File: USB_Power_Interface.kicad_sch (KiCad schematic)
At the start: 33 parts, among them CN501 GT-USB-7014D, U501 TPS2121, U502 TPSM82903

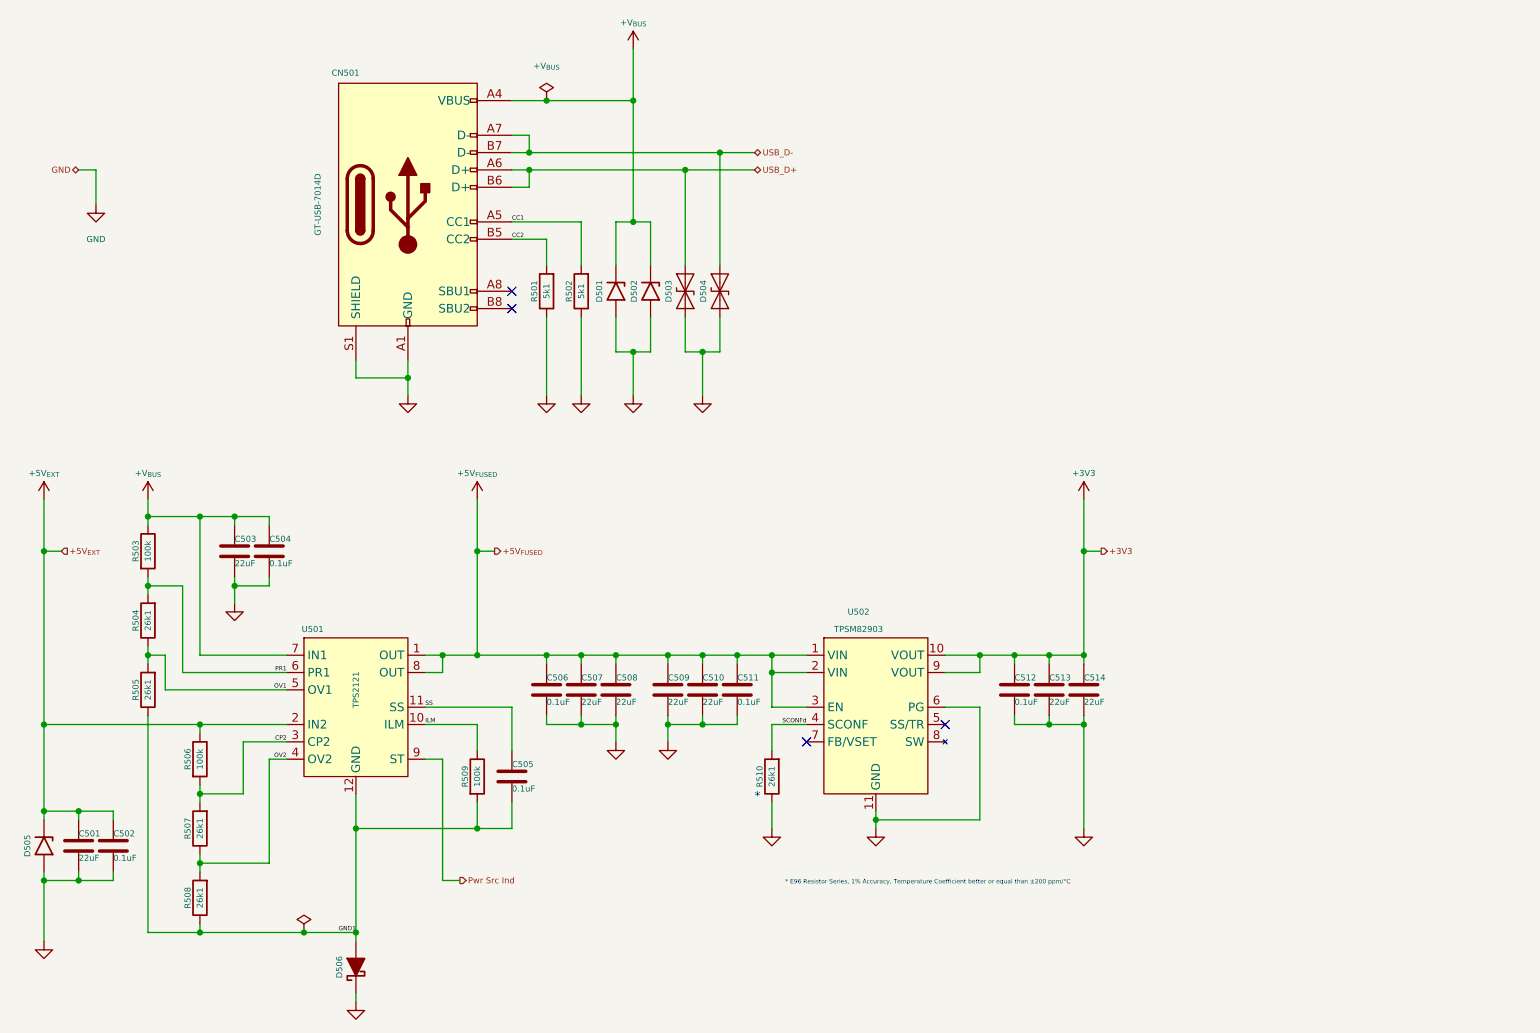
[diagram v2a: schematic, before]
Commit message: fixed hierarchical sheets; replaced pin headers with ESP32-S3_D1_Pico symbol
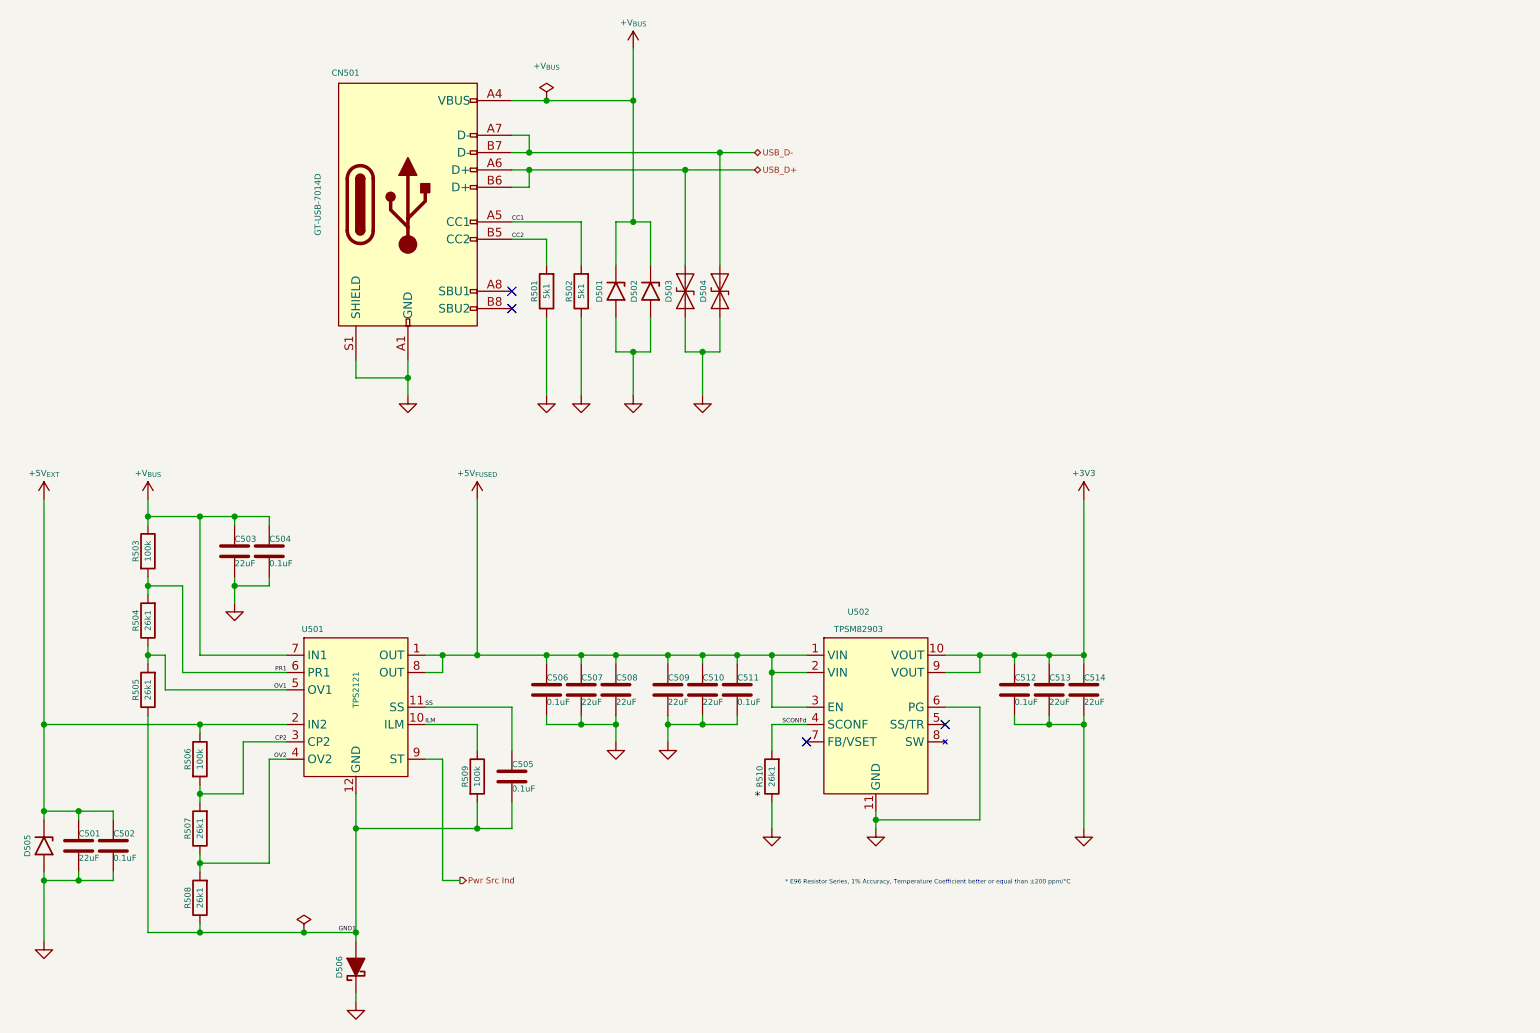
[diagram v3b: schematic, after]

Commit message: Update ESP32-S3 Pico D1-Main.kicad_sch, ESP32-S3 Pico D1.kicad_pcb, ESP32-S3 Pico D1.kicad_prl, and 7 more files
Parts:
- added +V501, +V503: +V_{BUS}, symbol My Power Management:+V (Local)
- added +V502, +V506: +5V_{EXT}, symbol My Power Management:+V (Local)
- added +V504, +V507: +5V_{FUSED}, symbol My Power Management:+V (Local)
- added +V505, +V508: +3V3, symbol My Power Management:+V (Local)
- added GND501, GND502, GND503, GND504, GND505, GND506, GND507, GND508, GND509, GND510, GND511, GND512, GND513, GND514: GND, symbol My Power Management:GND (Local)
- D506: footprint Personal_FootprintLibrary:DSN0603-2 -> My Package_Leadless:DFN0603-2
- R501, R502: footprint My Resistors:R_0201_Dense -> My Resistors:R_0201_Nominal
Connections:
- net +3V3: now also +V505.1, +V508.1
- net +5V_{EXT}: now also +V502.1, +V506.1
- net +5V_{FUSED}: now also +V504.1, +V507.1
- net +V_{BUS}: now also +V501.1, +V503.1
- net GND: now also GND501.1 (GND), GND502.1 (GND), GND503.1 (GND), GND504.1 (GND), GND505.1 (GND), GND506.1 (GND), GND507.1 (GND), GND508.1 (GND), GND509.1 (GND), GND510.1 (GND), GND511.1 (GND), GND512.1 (GND), GND513.1 (GND), GND514.1 (GND)
